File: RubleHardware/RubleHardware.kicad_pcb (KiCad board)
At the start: 4 copper layers, 56.5 x 75.4 mm, 46 parts, among them IC1 LTC3780EUH#PBF, J1_IN1 Conn_01x08_Male, J2_OUT1 Conn_01x08_Male

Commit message: feat: First board revision
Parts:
- moved Cin1 33.1 mm to (168.3, 100.2), turned to 90 degrees
- moved Cb1 31.8 mm to (178.3, 84.5), turned to 180 degrees
- moved Cin4 23.7 mm to (174.7, 100.3), turned to -90 degrees
- moved C2 23.0 mm to (186.6, 88.1), turned to 180 degrees
- moved C1 21.9 mm to (188.4, 91.6), turned to -90 degrees
- moved R2 21.6 mm to (187.4, 91.5)
- moved J1_IN1 18.2 mm to (181.5, 114.0)
- moved H3 18.1 mm to (188.0, 113.0)
- moved H4 17.4 mm to (162.5, 113.0)
- moved Css1 17.1 mm to (183.3, 91.0)
- moved Ca1 16.9 mm to (179.5, 90.6)
- moved Cin3 14.8 mm to (180.8, 100.3), turned to -90 degrees
- moved TP1 12.9 mm to (161.1, 72.6)
- moved TP2 9.09 mm to (161.1, 97.5)
- moved Cin2 6.12 mm to (186.7, 100.3), turned to -90 degrees
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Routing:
- net /CAN+: track 0.00 -> 60.4 mm
- net /CAN-: track 0.00 -> 53.5 mm
- net /TG1: track 0.00 -> 31.4 mm, vias 0 -> 2
- net /ICVIN: track 0.00 -> 17.2 mm
- net GND: track 22.5 -> 34.9 mm, vias 4 -> 8
- net Net-(Da1-K): track 6.29 -> 11.8 mm
- net Net-(IC1-ITH): track 0.00 -> 5.00 mm
- net /SW2: track 12.1 -> 14.1 mm
- net Net-(Db1-K): track 4.61 -> 6.31 mm
- net /TG2: track 25.1 -> 26.2 mm
- net /BG1: track 8.99 -> 10.1 mm
- net Net-(IC1-SS): track 0.00 -> 1.07 mm
- net Net-(C1-Pad2): track 0.00 -> 0.99 mm
- net Net-(JP1-A): track 2.61 -> 3.40 mm
- net Net-(IC1-PGOOD): track 7.25 -> 7.94 mm
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- added copper zone on In2.Cu, net +3V3
- added copper zone on F.Cu, net /ICVIN
- added copper zone on B.Cu, net GND
- added copper zone on F.Cu, net GND
- added copper zone on In1.Cu, net GND
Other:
- board size 56.5 x 75.4 mm -> 33.5 x 58 mm
- board text added: "12V"
- board text added: "24V"
- board text added: "PGOOD"
- board text added: "RSENS"

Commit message: feat: Board V2
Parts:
- moved Cin2 45.3 mm to (141.6, 95.3)
- moved Cin1 33.7 mm to (134.9, 95.2)
- moved Cin3 32.5 mm to (148.6, 95.5)
- moved H4 29.9 mm to (134.0, 104.0)
- moved H1 29.1 mm to (134.0, 69.0)
- moved R3 28.7 mm to (136.7, 82.3), turned to 180 degrees
- moved D1 25.7 mm to (138.2, 81.8), turned to 90 degrees
- moved Cout1 24.5 mm to (142.7, 82.3), turned to -90 degrees
- moved Cout2 23.9 mm to (152.4, 82.1), turned to -90 degrees
- moved Cout3 23.8 mm to (145.4, 82.4), turned to -90 degrees
- moved TP2 20.4 mm to (141.0, 101.0)
- moved Cin4 20.1 mm to (155.2, 95.5)
- moved TP1 19.2 mm to (142.1, 75.0)
- moved J1_IN1 9.53 mm to (179.3, 104.7)
- moved H3 9.00 mm to (188.0, 104.0)
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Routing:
- net +3V3: track 0.00 -> 58.5 mm
- net /CAN-: track 53.5 -> 91.0 mm
- net /CAN+: track 60.4 -> 31.5 mm
- net GND: track 34.9 -> 25.7 mm, vias 8 -> 34
- net /INTVCC: track 26.1 -> 30.0 mm
- net /SENS-: track 13.4 -> 17.2 mm, vias 0 -> 2
- net Net-(Db1-K): track 6.31 -> 8.37 mm
- net /SW2: track 14.1 -> 13.1 mm, vias 2 -> 0
- net Net-(Da1-K): track 11.8 -> 12.5 mm
- net /ICVOUT: track 18.8 -> 18.2 mm, vias 0 -> 2
- net Net-(IC1-PGOOD): track 7.94 -> 7.42 mm
- net /BG1: track 10.1 -> 9.68 mm, vias 0 -> 2
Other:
- board size 33.5 x 58 mm -> 62 x 43 mm

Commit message: feat: v3 almost complete
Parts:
- added C4: 100nF, Capacitor_SMD:C_0603_1608Metric, F.Cu at (168.2, 82.1)
- added R4: 10k, Resistor_SMD:R_0402_1005Metric, F.Cu at (173.4, 85.7)
- Ca1: value 0.22uF -> 1uF
- Cb1: value 0.22u -> 1uF
- Cout1: footprint Capacitor_SMD:C_0402_1005Metric -> iclr:CAPC1608X90N
- moved H2 70.2 mm to (131.0, 110.0)
- moved J1_IN1 44.3 mm to (154.0, 68.3), turned to 0 degrees
- moved J2_OUT1 43.5 mm to (166.3, 111.7), turned to 180 degrees
- moved H4 39.5 mm to (173.0, 110.0)
- moved H3 37.2 mm to (173.0, 70.0)
- moved TP1 28.1 mm to (150.0, 102.0)
- moved Cout2 26.6 mm to (141.6, 106.4), turned to 180 degrees
- moved D3 24.6 mm to (148.6, 96.7), turned to 180 degrees
- moved Cin1 24.3 mm to (145.0, 73.0), turned to 180 degrees
- moved TP2 22.2 mm to (144.0, 79.0)
- moved R1_24v1 21.6 mm to (169.4, 78.5), turned to 0 degrees
- moved Cin4 21.4 mm to (136.0, 85.9), turned to 0 degrees
- moved Cb1 21.3 mm to (158.6, 89.0), turned to 180 degrees
- moved Ca1 20.5 mm to (158.8, 93.0), turned to 180 degrees
- moved D4 19.6 mm to (155.6, 96.6), turned to 90 degrees
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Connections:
- B1 pad 1: /SENS- -> /SENS+
- B1 pad 2: /SENS- -> /SENS+
- B1 pad 3: /SENS- -> /SENS+
- B1 pad A1: /SENS- -> /SENS+
- C3 pad 1: /SENS- -> /SENS+
- C3 pad 2: /SENS- -> /SENS+
- C3 pad 3: /SENS- -> /SENS+
- C3 pad A1: /SENS- -> /SENS+
- D2 pad 1: /SENS- -> /SENS+
- D2 pad 2: /SENS- -> /SENS+
- IC1 pad 11: GND -> Net-(IC1-STBYMD)
- IC1 pad 8: unconnected-(IC1-PLLFTR-Pad8) -> Net-(IC1-PLLFTR)
- RSENS+1 pad 1: GND -> /SENS+
- RSENS-1 pad 1: /SENS- -> GND
- Rsense1 pad 2: /SENS- -> /SENS+
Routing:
- net /CAN+: track 31.5 -> 95.4 mm
- net +3V3: track 58.5 -> 0.00 mm
- net /ICVIN: track 17.2 -> 54.5 mm, vias 0 -> 23
- net /SENS+: track 0.00 -> 27.3 mm, vias 0 -> 7
- net GND: track 25.7 -> 49.7 mm, vias 34 -> 44
- net /SENS-: track 17.2 -> 0.00 mm, vias 2 -> 0
- net /ICVOUT: track 18.2 -> 29.5 mm, vias 2 -> 16
- net /TG1: track 31.4 -> 23.8 mm
- net Net-(IC1-VOSENSE): track 6.79 -> 14.1 mm
- net /SW2: track 13.1 -> 18.7 mm
- net /SW1: track 13.6 -> 19.0 mm, vias 2 -> 0
- net Net-(IC1-PGOOD): track 7.42 -> 2.35 mm
- net /TG2: track 26.2 -> 21.3 mm
- net Net-(IC1-VIN): track 10.4 -> 5.80 mm, vias 2 -> 0
- net Net-(Db1-K): track 8.37 -> 13.0 mm, vias 0 -> 2
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- added copper zone on B.Cu, net /ICVIN
- added copper zone on B.Cu, net /ICVOUT
- added copper zone on B.Cu, net /SENS+
- added copper zone on F.Cu, net /SENS+
- removed copper zone on F.Cu, net /SENS-
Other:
- board size 62 x 43 mm -> 52 x 50 mm
- board text removed: "12V"
- board text removed: "24V"
- board text removed: "PGOOD"
- board text removed: "PWR"
- board text removed: "RSENS"

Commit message: feat: V0.3 ready
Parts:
- added G***: LOGO, RubleHardware:Stonks, F.Cu at (158.0, 91.5)
- moved C4 0.82 mm to (167.4, 81.8)
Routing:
- net Net-(IC1-STBYMD): track 3.38 -> 4.00 mm
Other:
- board text added: "12V"
- board text added: "24V"
- board text added: "B"
- board text added: "E"
- board text added: "Input"
- board text added: "L"
- board text added: "Output"
- board text added: "PBad"
- board text added: "Power"
- board text added: "R"
- board text added: "Riley Horrix"
- board text added: "U"
- board text added: "Vin"
- board text added: "Vout"
- board text added: "niversal"
- board text added: "oad"
- board text added: "obust"
- board text added: "qualiser"
- board text added: "uck-Boost"
- board text added: "v1.0"

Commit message: trying something out
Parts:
- Cin2, Cin3, Cin4: footprint iclr:CAPC6050X550N -> iclr:CAPC2012X145N
- moved TP1 23.0 mm to (173.0, 102.0)
- moved Cout1 17.8 mm to (156.0, 92.3), turned to 90 degrees
- moved Cin3 17.6 mm to (149.0, 81.0), turned to 90 degrees
- moved H4 17.3 mm to (190.0, 107.0)
- moved H3 17.0 mm to (190.0, 71.0)
- moved Cout3 15.3 mm to (154.0, 92.0), turned to 90 degrees
- moved R3 15.1 mm to (151.0, 92.0), turned to 90 degrees
- moved A1 15.0 mm to (163.6, 82.9)
- moved B1 15.0 mm to (169.8, 87.7)
- moved C1 15.0 mm to (190.8, 90.0)
- moved C2 15.0 mm to (188.5, 90.0)
- moved C3 15.0 mm to (169.8, 92.3)
- moved C4 15.0 mm to (182.4, 82.3)
- moved CSENS1 15.0 mm to (187.1, 92.8)
- moved Ca1 15.0 mm to (173.7, 93.5)
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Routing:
- net /CAN+: track 95.4 -> 0.00 mm
- net /CAN-: track 92.1 -> 0.00 mm
- net /ICVIN: track 54.5 -> 3.09 mm, vias 23 -> 2
- net /ICVOUT: track 29.5 -> 1.10 mm, vias 16 -> 1
- net GND: vias 44 -> 21
- removed copper zone on In2.Cu, net +3V3
- removed copper zone on B.Cu, net /ICVIN
- removed copper zone on B.Cu, net /ICVOUT
- removed copper zone on B.Cu, net GND
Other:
- board size 52 x 50 mm -> 62 x 46 mm

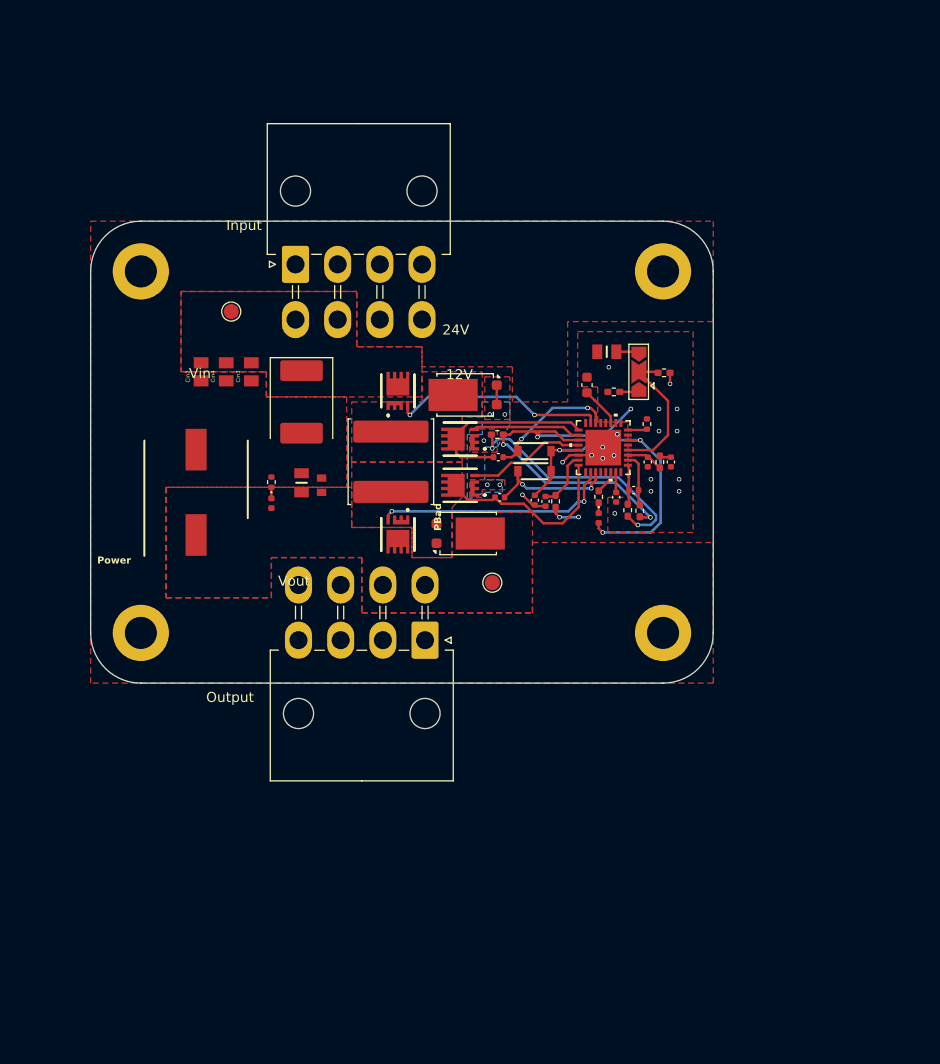
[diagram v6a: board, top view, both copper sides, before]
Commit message: feat: Redesign completer
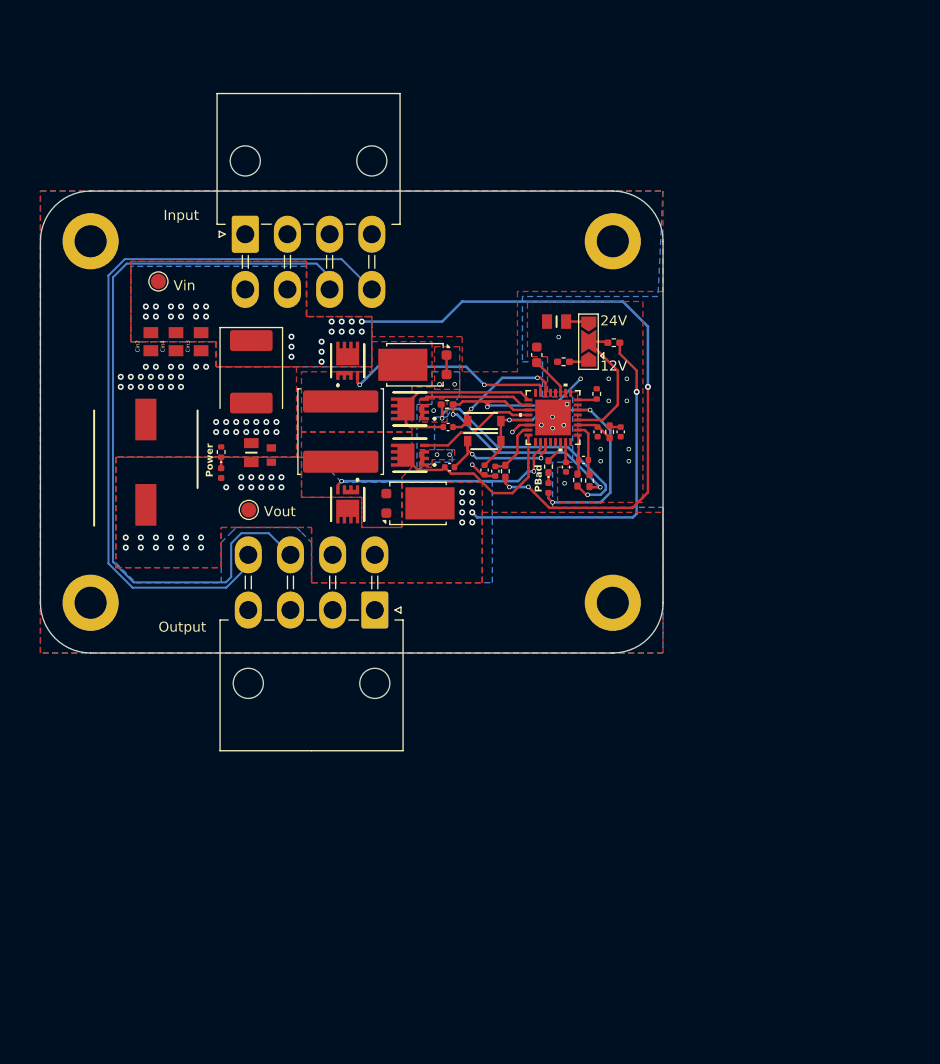
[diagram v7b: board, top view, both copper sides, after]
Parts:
- moved TP1 25.3 mm to (148.8, 94.8)
- moved TP2 7.85 mm to (139.8, 72.0)
- moved A1 5.83 mm to (158.6, 79.9)
- moved B1 5.83 mm to (164.8, 84.7)
- moved C1 5.83 mm to (185.8, 87.0)
- moved C2 5.83 mm to (183.5, 87.0)
- moved C3 5.83 mm to (164.8, 89.3)
- moved C4 5.83 mm to (177.4, 79.3)
- moved CSENS1 5.83 mm to (182.1, 89.8)
- moved Ca1 5.83 mm to (168.7, 90.5)
- moved Cb1 5.83 mm to (168.6, 86.5)
- moved Cf1 5.83 mm to (173.3, 90.9)
- moved Cin1 5.83 mm to (149.0, 81.0)
- moved Cin2 5.83 mm to (139.0, 78.0)
- moved Cin3 5.83 mm to (144.0, 78.0)
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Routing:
- net /CAN-: track 0.00 -> 75.7 mm
- net /CAN+: track 0.00 -> 73.7 mm
- net /ICVIN: track 3.09 -> 63.4 mm, vias 2 -> 29
- net /ICVOUT: track 1.10 -> 34.5 mm, vias 1 -> 32
- net GND: vias 21 -> 55
- added copper zone on In2.Cu, net +3V3
- added copper zone on B.Cu, net /ICVIN
- added copper zone on B.Cu, net /ICVOUT
- added copper zone on B.Cu, net GND

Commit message: feat: v0.4 ready
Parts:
- added R5: 15k, Resistor_SMD:R_0402_1005Metric, F.Cu at (190.7, 83.2)
- Rsense1: value 1.9m -> 5m; footprint Resistor_SMD:R_0402_1005Metric_Pad0.72x0.64mm_HandSolder -> iclr:RESC6432X67N
- moved H3 8.02 mm to (193.0, 67.5)
- moved H4 8.02 mm to (193.0, 104.5)
- moved RSENS+1 6.89 mm to (188.1, 89.8)
- moved RSENS-1 6.77 mm to (189.1, 89.8)
- moved CSENS1 6.72 mm to (188.6, 88.2)
- moved C1 6.53 mm to (192.3, 86.8)
- moved C2 6.53 mm to (190.0, 86.8)
- moved C4 6.53 mm to (184.0, 79.1)
- moved Cf1 6.53 mm to (179.8, 90.7)
- moved Css1 6.53 mm to (186.9, 90.3)
- moved Cvcc1 6.53 mm to (178.8, 90.6)
- moved Da1 6.53 mm to (178.7, 87.7)
- moved Db1 6.53 mm to (178.7, 85.7)
- moved IC1 6.53 mm to (185.6, 85.4)
- moved JP1 6.53 mm to (189.1, 77.8)
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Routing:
- net /TG2: track 21.3 -> 31.8 mm
- net Net-(Db1-K): track 13.0 -> 21.0 mm
- net /BG2: track 10.8 -> 18.4 mm, vias 0 -> 2
- net /BG1: track 11.8 -> 18.5 mm
- net /TG1: track 23.8 -> 30.4 mm
- net /SW1: track 19.0 -> 25.3 mm
- net Net-(Da1-K): track 13.4 -> 19.0 mm
- net /SW2: track 18.7 -> 23.9 mm, vias 0 -> 2
- net GND: track 49.7 -> 54.5 mm, vias 55 -> 47
- net /ICVOUT: track 34.5 -> 38.3 mm, vias 32 -> 26
- net /ICVIN: track 63.4 -> 66.2 mm, vias 29 -> 17
- net /SENS+: track 27.3 -> 25.1 mm
- net Net-(IC1-SENSE-): track 5.34 -> 3.39 mm
- net Net-(IC1-VOSENSE): track 14.1 -> 15.9 mm
- net Net-(IC1-SENSE+): track 3.98 -> 2.11 mm
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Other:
- board size 62 x 46 mm -> 63 x 43 mm
